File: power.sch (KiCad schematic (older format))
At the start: 14 parts, among them J5 Jack-12V AC, J6 Ext. GND, SW1 SW_SPST, U4 LM7812_TO220, U5 LM7912_TO220

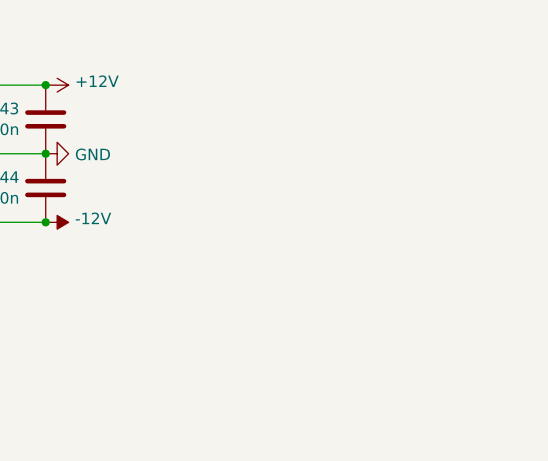
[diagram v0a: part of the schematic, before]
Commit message: full connection before relayouting labels
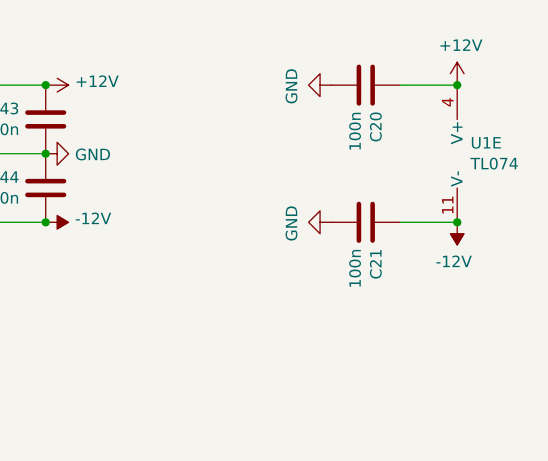
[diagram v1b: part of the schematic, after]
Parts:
- added C20, C21: 100n, Capacitor_THT:C_Rect_L7.2mm_W2.5mm_P5.00mm_FKS2_FKP2_MKS2_MKP2, symbol Device:C
- added U1: TL074, Package_DIP:DIP-14_W7.62mm_LongPads, symbol Amplifier_Operational:TL074
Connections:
- net +12V: now also C20.1, U1.4 (V+)
- net -12V: now also C21.1, U1.11 (V-)
- net GND: now also C20.2, C21.2
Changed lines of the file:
@@
 $Descr A4 11693 8268
 encoding utf-8
-Sheet 3 3
+Sheet 3 4
 Title ""
 Date ""
@@
 Wire Wire Line
 	3850 3000 3750 3000
+$Comp
+L Amplifier_Operational:TL074 U1
+U 5 1 5F861DD1
+P 6300 1600
+F 0 "U1" H 6258 1646 50  0000 L CNN
+F 1 "TL074" H 6258 1555 50  0000 L CNN
+F 2 "Package_DIP:DIP-14_W7.62mm_LongPads" H 6250 1700 50  0001 C CNN
+F 3 "http://www.ti.com/lit/ds/symlink/tl071.pdf" H 6350 1800 50  0001 C CNN
+	5    6300 1600
+	1    0    0    -1
+$EndComp
+$Comp
+L power:+12V #PWR?
+U 1 1 5F861DD7
+P 6200 1300
+F 0 "#PWR?" H 6200 1150 50  0001 C CNN
+F 1 "+12V" H 6215 1473 50  0000 C CNN
+F 2 "" H 6200 1300 50  0001 C CNN
+F 3 "" H 6200 1300 50  0001 C CNN
+	1    6200 1300
+	1    0    0    -1
+$EndComp
+$Comp
+L power:-12V #PWR?
+U 1 1 5F861DDD
+P 6200 1900
+F 0 "#PWR?" H 6200 2000 50  0001 C CNN
+F 1 "-12V" H 6215 2073 50  0000 C CNN
+F 2 "" H 6200 1900 50  0001 C CNN
+F 3 "" H 6200 1900 50  0001 C CNN
+	1    6200 1900
+	-1   0    0    1
+$EndComp
+$Comp
+L Device:C C?
+U 1 1 5F861DE3
+P 5800 1300
+AR Path="/5F35ADD1/5F861DE3" Ref="C?"  Part="1"
+AR Path="/5F861DE3" Ref="C?"  Part="1"
+AR Path="/5F7BBEAA/5F861DE3" Ref="C20"  Part="1"
+F 0 "C20" H 5915 1346 50  0000 L CNN
+F 1 "100n" H 5915 1255 50  0000 L CNN
+F 2 "Capacitor_THT:C_Rect_L7.2mm_W2.5mm_P5.00mm_FKS2_FKP2_MKS2_MKP2" H 5838 1150 50  0001 C CNN
+F 3 "~" H 5800 1300 50  0001 C CNN
+	1    5800 1300
+	0    1    1    0
+$EndComp
+$Comp
+L power:GND #PWR?
+U 1 1 5F861DE9
+P 5650 1300
+AR Path="/5F35ADD1/5F861DE9" Ref="#PWR?"  Part="1"
+AR Path="/5F861DE9" Ref="#PWR?"  Part="1"
+AR Path="/5F7BBEAA/5F861DE9" Ref="#PWR?"  Part="1"
+F 0 "#PWR?" H 5650 1050 50  0001 C CNN
+F 1 "GND" H 5655 1127 50  0000 C CNN
+F 2 "" H 5650 1300 50  0001 C CNN
+F 3 "" H 5650 1300 50  0001 C CNN
+	1    5650 1300
+	0    1    1    0
+$EndComp
+$Comp
+L Device:C C?
+U 1 1 5F861DEF
+P 5800 1900
+AR Path="/5F35ADD1/5F861DEF" Ref="C?"  Part="1"
+AR Path="/5F861DEF" Ref="C?"  Part="1"
+AR Path="/5F7BBEAA/5F861DEF" Ref="C21"  Part="1"
+F 0 "C21" H 5915 1946 50  0000 L CNN
+F 1 "100n" H 5915 1855 50  0000 L CNN
+F 2 "Capacitor_THT:C_Rect_L7.2mm_W2.5mm_P5.00mm_FKS2_FKP2_MKS2_MKP2" H 5838 1750 50  0001 C CNN
+F 3 "~" H 5800 1900 50  0001 C CNN
+	1    5800 1900
+	0    1    1    0
+$EndComp
+$Comp
+L power:GND #PWR?
+U 1 1 5F861DF5
+P 5650 1900
+AR Path="/5F35ADD1/5F861DF5" Ref="#PWR?"  Part="1"
+AR Path="/5F861DF5" Ref="#PWR?"  Part="1"
+AR Path="/5F7BBEAA/5F861DF5" Ref="#PWR?"  Part="1"
+F 0 "#PWR?" H 5650 1650 50  0001 C CNN
+F 1 "GND" H 5655 1727 50  0000 C CNN
+F 2 "" H 5650 1900 50  0001 C CNN
+F 3 "" H 5650 1900 50  0001 C CNN
+	1    5650 1900
+	0    1    1    0
+$EndComp
+Wire Wire Line
+	5950 1900 6200 1900
+Wire Wire Line
+	5950 1300 6200 1300
+Connection ~ 6200 1300
+Connection ~ 6200 1900
 $EndSCHEMATC

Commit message: add panels
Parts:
- removed C42: 1u, Capacitor_THT:C_Rect_L7.0mm_W6.0mm_P5.00mm, symbol Device:C
- C40, C41: value 4700u -> 3300u; footprint Capacitor_THT:C_Radial_D16.0mm_H31.5mm_P7.50mm -> Capacitor_THT:CP_Radial_D13.0mm_P5.00mm
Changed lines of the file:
@@
 AR Path="/5F7BBEAA/5F814ECD" Ref="C40"  Part="1"
 F 0 "C40" H 3218 1496 50  0000 L CNN
-F 1 "4700u" H 3218 1405 50  0000 L CNN
-F 2 "Capacitor_THT:C_Radial_D16.0mm_H31.5mm_P7.50mm" H 3138 1300 50  0001 C CNN
+F 1 "3300u" H 3218 1405 50  0000 L CNN
+F 2 "Capacitor_THT:CP_Radial_D13.0mm_P5.00mm" H 3138 1300 50  0001 C CNN
 F 3 "~" H 3100 1450 50  0001 C CNN
 	1    3100 1450
@@
 AR Path="/5F7BBEAA/5F814ED3" Ref="C41"  Part="1"
 F 0 "C41" H 3218 1796 50  0000 L CNN
-F 1 "4700u" H 3218 1705 50  0000 L CNN
-F 2 "Capacitor_THT:C_Radial_D16.0mm_H31.5mm_P7.50mm" H 3138 1600 50  0001 C CNN
+F 1 "3300u" H 3218 1705 50  0000 L CNN
+F 2 "Capacitor_THT:CP_Radial_D13.0mm_P5.00mm" H 3138 1600 50  0001 C CNN
 F 3 "~" H 3100 1750 50  0001 C CNN
 	1    3100 1750
-	-1   0    0    -1
-$EndComp
-$Comp
-L Device:C C?
-U 1 1 5F814ED9
-P 3450 1750
-AR Path="/5F814ED9" Ref="C?"  Part="1"
-AR Path="/5F7FCB67/5F814ED9" Ref="C?"  Part="1"
-AR Path="/5F7BBEAA/5F814ED9" Ref="C42"  Part="1"
-F 0 "C42" H 3565 1796 50  0000 L CNN
-F 1 "1u" H 3565 1705 50  0000 L CNN
-F 2 "Capacitor_THT:C_Rect_L7.0mm_W6.0mm_P5.00mm" H 3488 1600 50  0001 C CNN
-F 3 "~" H 3450 1750 50  0001 C CNN
-	1    3450 1750
 	-1   0    0    -1
 $EndComp
@@
 	-1   0    0    -1
 $EndComp
-Wire Wire Line
-	3100 1600 3450 1600
 Connection ~ 3100 1600
-Wire Wire Line
-	3450 1600 3850 1600
-Connection ~ 3450 1600
 Connection ~ 4400 1600
-Wire Wire Line
-	3550 1900 3450 1900
-Wire Wire Line
-	3450 1900 3100 1900
-Connection ~ 3450 1900
 Wire Wire Line
 	3100 1900 2850 1900
@@
 Connection ~ 6200 1300
 Connection ~ 6200 1900
+Wire Wire Line
+	3100 1600 3850 1600
+Wire Wire Line
+	3100 1900 3550 1900
 $EndSCHEMATC
